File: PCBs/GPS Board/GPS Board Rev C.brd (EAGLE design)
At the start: 4 parts

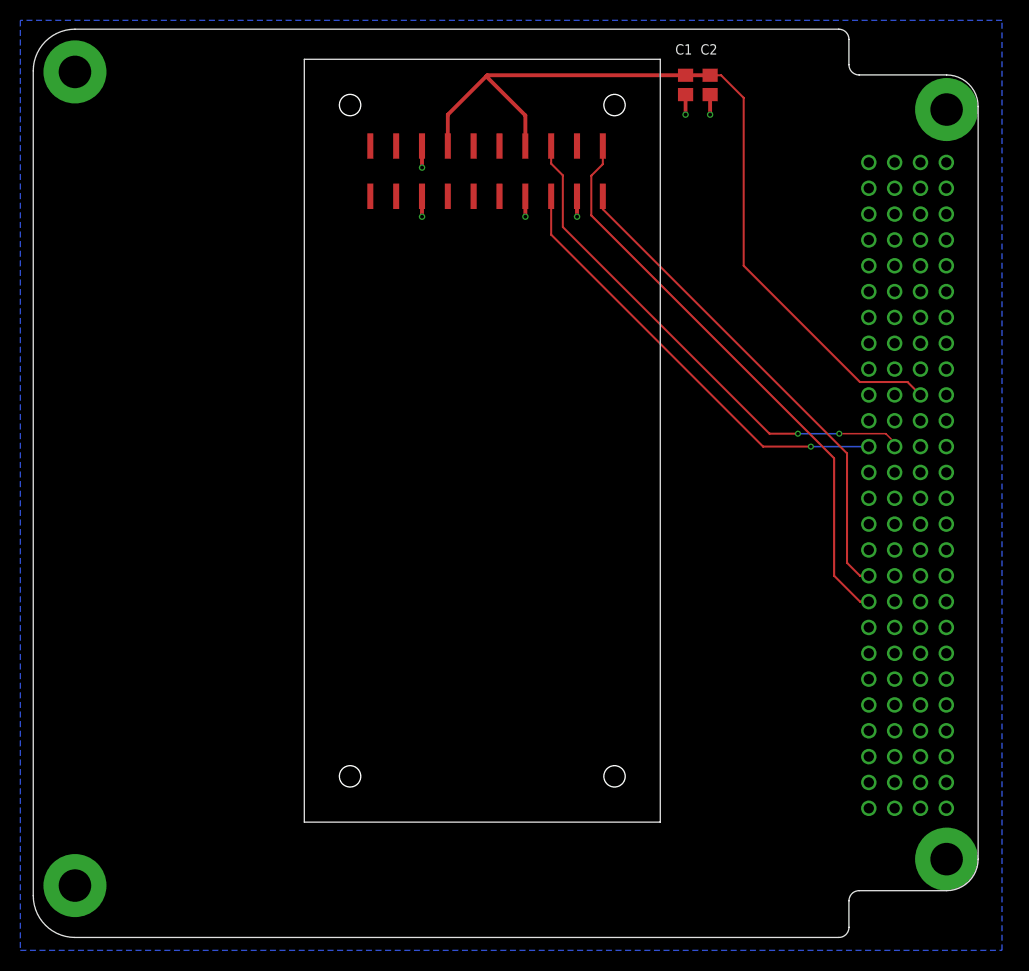
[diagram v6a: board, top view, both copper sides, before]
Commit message: Update GPS board to use new library
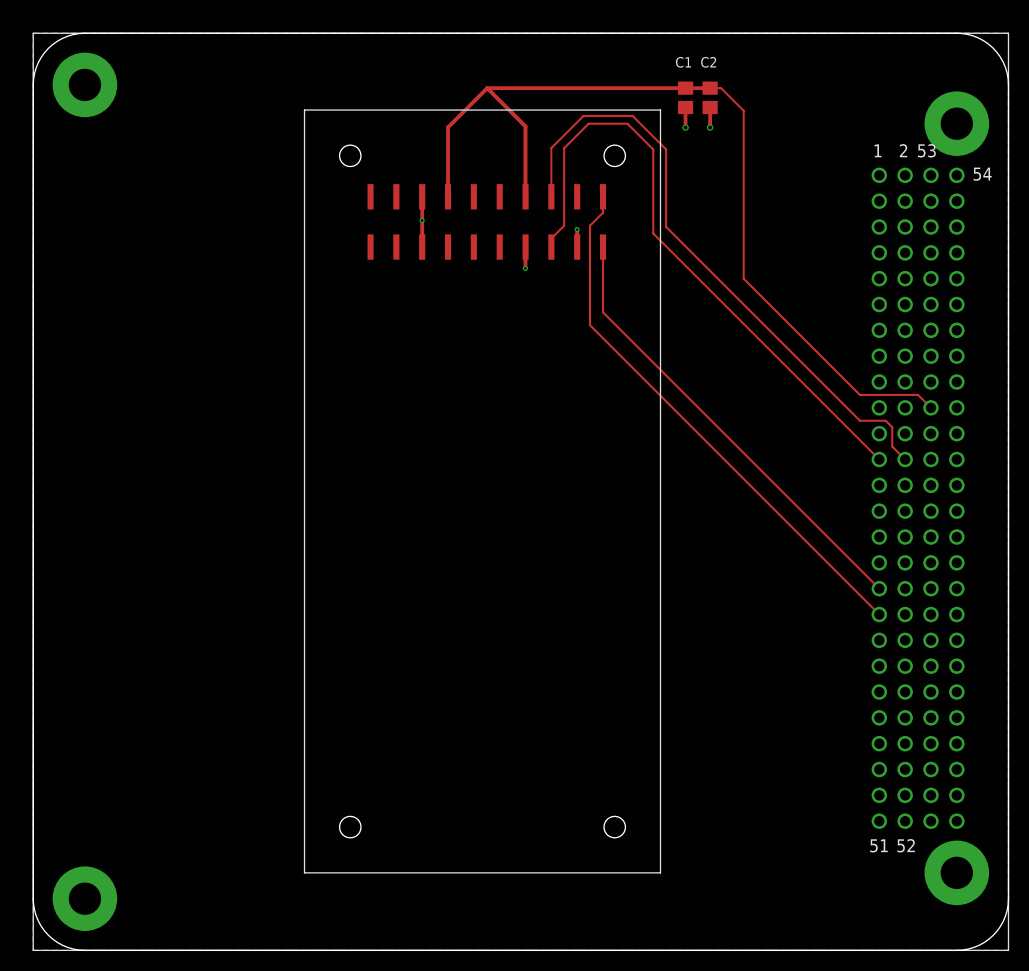
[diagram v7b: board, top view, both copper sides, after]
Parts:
- U$1: value PINAVL1 -> PINAV-L1; device pinavl1:PINAV-L1 -> Cubesat:PINAV-L1
- U$2: value PC104 -> PC104_GPS; device Cubesat:PC104 -> Cubesat:PC104_GPS
- moved U$1 45.5 mm to (26.7, 7.62), turned to 0 degrees
- moved C1 1.27 mm to (64.1, 83.8)
- moved C2 1.27 mm to (66.5, 83.8)
- moved U$2 1.27 mm to (0.00, 0.00)
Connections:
- net GND: now also U$2.100, U$2.61, U$2.66, U$2.69, U$2.73, U$2.74, U$2.81, U$2.82, U$2.84, U$2.99; no longer U$2.P$100, U$2.P$61, U$2.P$66, U$2.P$69, U$2.P$73, U$2.P$74, U$2.P$81, U$2.P$82, U$2.P$84, U$2.P$99
- net PF: now also U$2.24; no longer U$2.P$24
- net RX: now also U$2.35; no longer U$2.P$35
- net SW9: now also U$2.71; no longer U$2.P$71
- net TX: now also U$2.33; no longer U$2.P$33
- net VPP: now also U$2.23; no longer U$2.P$23
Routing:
- net VPP: track 43.6 -> 60.7 mm, vias 1 -> 0
- net PF: track 50.2 -> 60.5 mm, vias 2 -> 0
- net SW9: track 82.3 -> 90.8 mm
- net TX: track 48.7 -> 44.8 mm
- net RX: track 57.1 -> 53.4 mm
- net GND: track 12.1 -> 12.7 mm, vias 6 -> 5
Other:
- board outline added: 95.9 x 90.2 mm

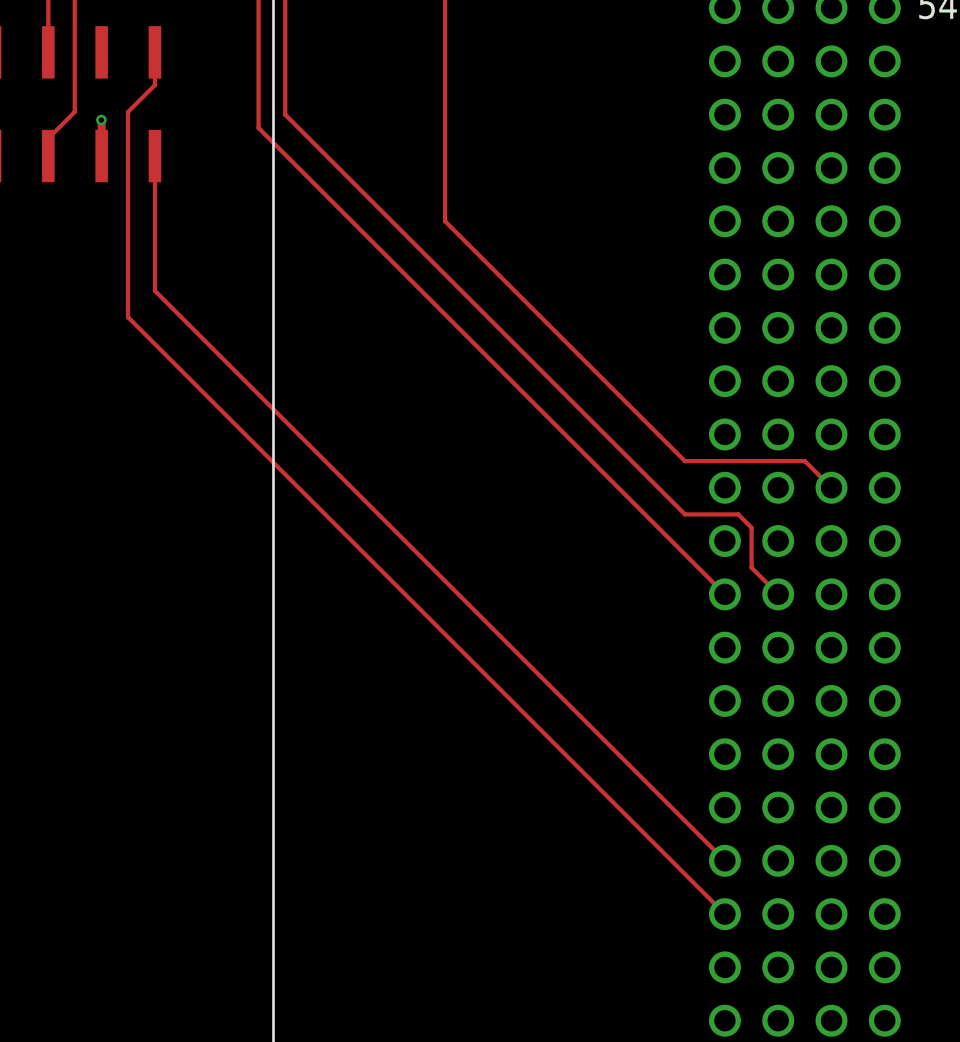
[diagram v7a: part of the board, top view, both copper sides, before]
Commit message: Use common PC104 footprint with dimensions set per board
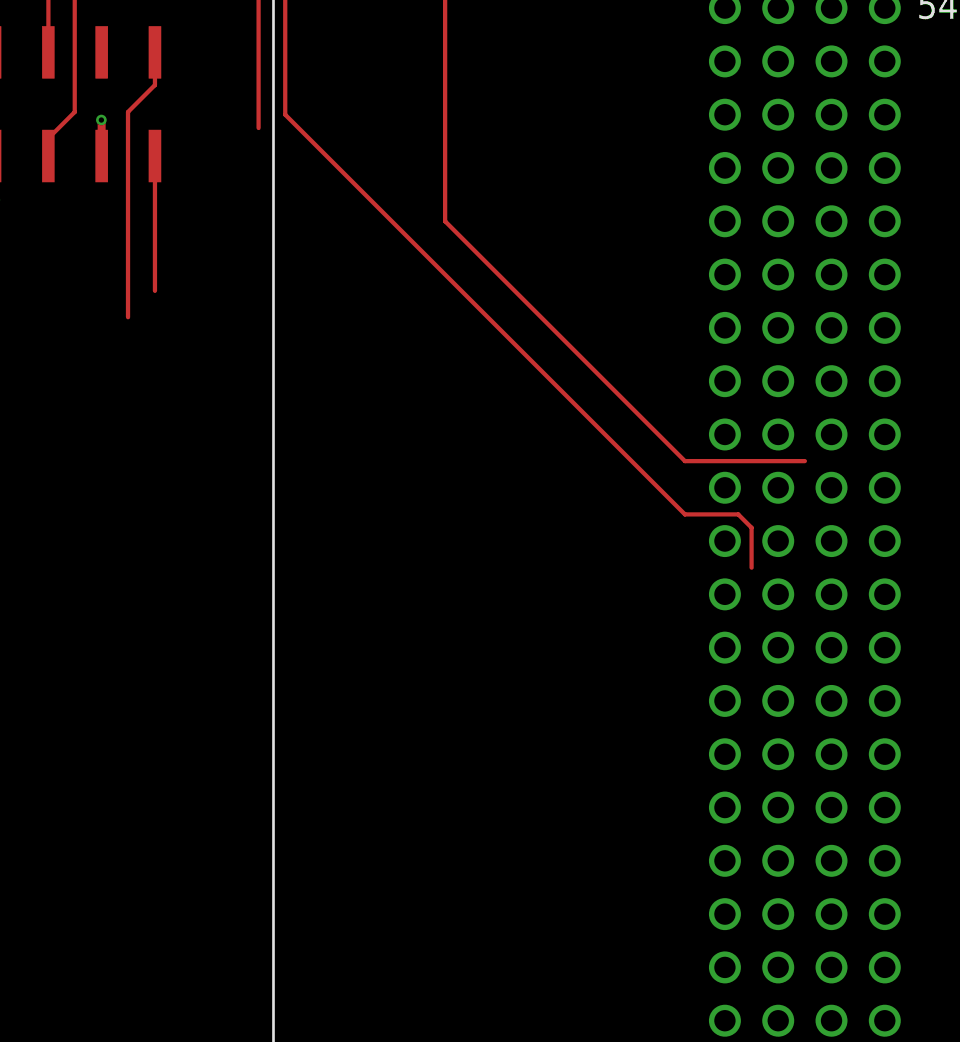
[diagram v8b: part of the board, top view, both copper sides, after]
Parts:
- U$2: value PC104_GPS -> PC104_NO_DIMENSION; device Cubesat:PC104_GPS -> Cubesat:PC104_NO_DIMENSION
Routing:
- net RX: track 53.4 -> 13.2 mm
- net TX: track 44.8 -> 6.43 mm
- net VPP: track 60.7 -> 29.3 mm
- net PF: track 60.5 -> 58.7 mm
- net SW9: track 90.8 -> 89.0 mm
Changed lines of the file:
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@@
 <board>
 <plain>
+<wire x1="0" y1="85.09" x2="0" y2="5.08" width="0.127" layer="20"/>
+<wire x1="0" y1="5.08" x2="5.08" y2="0" width="0.127" layer="20" curve="90"/>
+<wire x1="5.08" y1="0" x2="90.805" y2="0" width="0.127" layer="20"/>
+<wire x1="90.805" y1="0" x2="95.885" y2="5.08" width="0.127" layer="20" curve="90"/>
+<wire x1="95.885" y1="5.08" x2="95.885" y2="85.09" width="0.127" layer="20"/>
+<wire x1="95.885" y1="85.09" x2="90.678" y2="90.17" width="0.127" layer="20" curve="91.414625"/>
+<wire x1="0" y1="85.09" x2="5.08" y2="90.17" width="0.127" layer="20" curve="-90"/>
+<wire x1="5.08" y1="90.17" x2="90.678" y2="90.17" width="0.127" layer="20"/>
 </plain>
 <attributes>
@@
 </element>
 <element name="U$1" library="Cubesat" package="PINAV-L1" value="PINAV-L1" x="26.67" y="7.62"/>
-<element name="U$2" library="Cubesat" package="PC104_GPS" value="PC104_GPS" x="0" y="0"/>
+<element name="U$2" library="Cubesat" package="PC104_NO_DIMENSION" value="PC104_NO_DIMENSION" x="0" y="0"/>
 </elements>
 <signals>
@@
 <contactref element="U$1" pad="8"/>
 <contactref element="U$1" pad="14"/>
-<contactref element="U$2" pad="71"/>
 <wire x1="40.78" y1="80.912" x2="44.638" y2="84.77" width="0.381" layer="1"/>
 <wire x1="40.78" y1="74.09" x2="40.78" y2="80.912" width="0.381" layer="1"/>
 <wire x1="48.4" y1="81.008" x2="44.638" y2="84.77" width="0.381" layer="1"/>
 <wire x1="48.4" y1="74.09" x2="48.4" y2="81.008" width="0.381" layer="1"/>
-<wire x1="88.265" y1="53.34" x2="86.995" y2="54.61" width="0.2032" layer="1"/>
 <wire x1="86.995" y1="54.61" x2="81.28" y2="54.61" width="0.2032" layer="1"/>
+<contactref element="U$2" pad="71"/>
+<wire x1="88.265" y1="53.34" x2="86.995" y2="54.61" width="0" layer="19" extent="1-1"/>
 </signal>
 <signal name="GND">
@@
 <wire x1="64.135" y1="82.87" x2="64.135" y2="80.899" width="0.381" layer="1"/>
 <via x="64.135" y="80.899" extent="1-16" drill="0.381"/>
+<wire x1="38.24" y1="74.09" x2="38.24" y2="69.15" width="0.381" layer="1"/>
+<via x="38.227" y="71.755" extent="1-16" drill="0.254"/>
+<wire x1="48.4" y1="69.15" x2="48.4" y2="67.069" width="0.381" layer="1"/>
+<wire x1="48.4" y1="67.069" x2="48.387" y2="67.056" width="0.381" layer="1"/>
+<via x="48.387" y="67.056" extent="1-16" drill="0.254"/>
+<wire x1="53.48" y1="70.853" x2="53.48" y2="69.15" width="0.381" layer="1"/>
+<via x="53.467" y="70.866" extent="1-16" drill="0.254"/>
+<wire x1="53.467" y1="70.866" x2="53.48" y2="70.853" width="0.381" layer="1"/>
 <contactref element="U$2" pad="61"/>
 <contactref element="U$2" pad="66"/>
@@
 <contactref element="U$2" pad="99"/>
 <contactref element="U$2" pad="100"/>
-<wire x1="38.24" y1="74.09" x2="38.24" y2="69.15" width="0.381" layer="1"/>
-<via x="38.227" y="71.755" extent="1-16" drill="0.254"/>
-<wire x1="48.4" y1="69.15" x2="48.4" y2="67.069" width="0.381" layer="1"/>
-<wire x1="48.4" y1="67.069" x2="48.387" y2="67.056" width="0.381" layer="1"/>
-<via x="48.387" y="67.056" extent="1-16" drill="0.254"/>
-<wire x1="53.48" y1="70.853" x2="53.48" y2="69.15" width="0.381" layer="1"/>
-<via x="53.467" y="70.866" extent="1-16" drill="0.254"/>
-<wire x1="53.467" y1="70.866" x2="53.48" y2="70.853" width="0.381" layer="1"/>
+<wire x1="64.135" y1="82.87" x2="66.548" y2="82.87" width="0" layer="19" extent="1-1"/>
+<wire x1="53.467" y1="70.866" x2="64.135" y2="80.899" width="0" layer="19" extent="1-1"/>
+<wire x1="48.4" y1="69.15" x2="53.48" y2="69.15" width="0" layer="19" extent="1-1"/>
+<wire x1="38.24" y1="69.15" x2="48.4" y2="69.15" width="0" layer="19" extent="1-1"/>
 <wire x1="38.227" y1="71.755" x2="38.24" y2="74.09" width="0" layer="19" extent="1-1"/>
+<wire x1="88.265" y1="66.04" x2="48.4" y2="67.069" width="0" layer="19" extent="1-1"/>
+<wire x1="90.805" y1="60.96" x2="88.265" y2="66.04" width="0" layer="19" extent="1-1"/>
+<wire x1="88.265" y1="55.88" x2="90.805" y2="60.96" width="0" layer="19" extent="1-1"/>
+<wire x1="88.265" y1="50.8" x2="88.265" y2="55.88" width="0" layer="19" extent="1-1"/>
+<wire x1="90.805" y1="50.8" x2="88.265" y2="50.8" width="0" layer="19" extent="1-1"/>
+<wire x1="90.805" y1="40.64" x2="90.805" y2="50.8" width="0" layer="19" extent="1-1"/>
+<wire x1="88.265" y1="40.64" x2="90.805" y2="40.64" width="0" layer="19" extent="1-1"/>
+<wire x1="90.805" y1="38.1" x2="90.805" y2="40.64" width="0" layer="19" extent="1-1"/>
+<wire x1="90.805" y1="17.78" x2="90.805" y2="38.1" width="0" layer="19" extent="1-1"/>
+<wire x1="88.265" y1="17.78" x2="90.805" y2="17.78" width="0" layer="19" extent="1-1"/>
 </signal>
 <signal name="VPP">
 <contactref element="U$1" pad="5"/>
-<contactref element="U$2" pad="23"/>
 <wire x1="50.94" y1="69.15" x2="50.94" y2="69.99" width="0.2032" layer="1"/>
 <wire x1="54.61" y1="81.28" x2="58.42" y2="81.28" width="0.2032" layer="1"/>
 <wire x1="58.42" y1="81.28" x2="60.96" y2="78.74" width="0.2032" layer="1"/>
 <wire x1="60.96" y1="78.74" x2="60.96" y2="70.485" width="0.2032" layer="1"/>
-<wire x1="60.96" y1="70.485" x2="83.185" y2="48.26" width="0.2032" layer="1"/>
 <wire x1="50.94" y1="69.99" x2="52.197" y2="71.247" width="0.2032" layer="1"/>
 <wire x1="52.197" y1="71.247" x2="52.197" y2="78.867" width="0.2032" layer="1"/>
 <wire x1="52.197" y1="78.867" x2="54.61" y2="81.28" width="0.2032" layer="1"/>
+<contactref element="U$2" pad="23"/>
+<wire x1="83.185" y1="48.26" x2="60.96" y2="70.485" width="0" layer="19" extent="1-1"/>
 </signal>
 <signal name="PF">
 <contactref element="U$1" pad="6"/>
-<contactref element="U$2" pad="24"/>
 <wire x1="50.94" y1="74.09" x2="50.94" y2="78.88" width="0.2032" layer="1"/>
 <wire x1="62.23" y1="71.12" x2="81.28" y2="52.07" width="0.2032" layer="1"/>
@@
 <wire x1="83.82" y1="52.07" x2="84.455" y2="51.435" width="0.2032" layer="1"/>
 <wire x1="84.455" y1="51.435" x2="84.455" y2="49.53" width="0.2032" layer="1"/>
-<wire x1="84.455" y1="49.53" x2="85.725" y2="48.26" width="0.2032" layer="1"/>
 <wire x1="50.94" y1="78.88" x2="54.102" y2="82.042" width="0.2032" layer="1"/>
 <wire x1="54.102" y1="82.042" x2="58.928" y2="82.042" width="0.2032" layer="1"/>
 <wire x1="58.928" y1="82.042" x2="62.23" y2="78.74" width="0.2032" layer="1"/>
 <wire x1="62.23" y1="78.74" x2="62.23" y2="71.12" width="0.2032" layer="1"/>
+<contactref element="U$2" pad="24"/>
+<wire x1="85.725" y1="48.26" x2="84.455" y2="49.53" width="0" layer="19" extent="1-1"/>
 </signal>
 <signal name="TX">
 <contactref element="U$1" pad="1"/>
+<wire x1="56.02" y1="69.15" x2="56.02" y2="62.725" width="0.2032" layer="1"/>
 <contactref element="U$2" pad="33"/>
-<wire x1="56.02" y1="69.15" x2="56.02" y2="62.725" width="0.2032" layer="1"/>
-<wire x1="56.02" y1="62.725" x2="83.185" y2="35.56" width="0.2032" layer="1"/>
+<wire x1="83.185" y1="35.56" x2="56.02" y2="62.725" width="0" layer="19" extent="1-1"/>
 </signal>
 <signal name="RX">
 <contactref element="U$1" pad="2"/>
-<contactref element="U$2" pad="35"/>
 <wire x1="56.02" y1="74.09" x2="56.02" y2="72.53" width="0.2032" layer="1"/>
-<wire x1="54.737" y1="61.468" x2="83.185" y2="33.02" width="0.2032" layer="1"/>
 <wire x1="56.02" y1="72.53" x2="54.737" y2="71.247" width="0.2032" layer="1"/>
 <wire x1="54.737" y1="71.247" x2="54.737" y2="61.468" width="0.2032" layer="1"/>
+<contactref element="U$2" pad="35"/>
+<wire x1="83.185" y1="33.02" x2="54.737" y2="61.468" width="0" layer="19" extent="1-1"/>
 </signal>
 </signals>
